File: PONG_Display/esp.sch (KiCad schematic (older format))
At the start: 15 parts, among them J8 ESP_Conn, J9 ESP_Prog_Conn, Q1 BSS138, Q2 BSS138, SW2 SW_Push, SW3 SW_Push_SPDT, SW4 SW_Push_SPDT

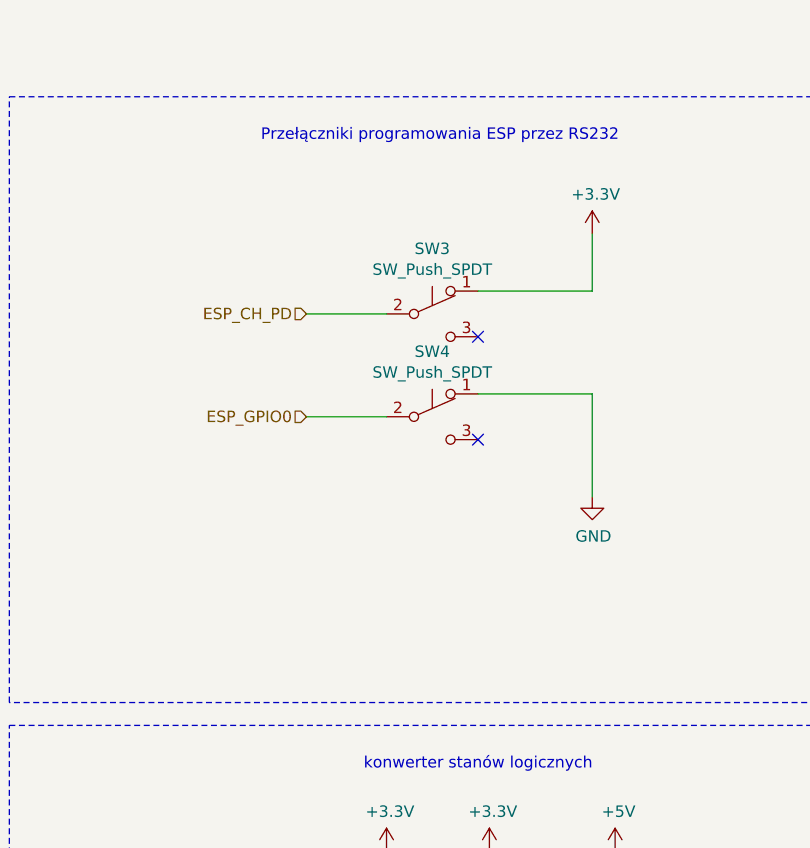
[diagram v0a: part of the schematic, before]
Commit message: Updated GPIO pins in ESP schematic
Connected GPIO2 to VDD with pull-up resistor and changed switches wiring
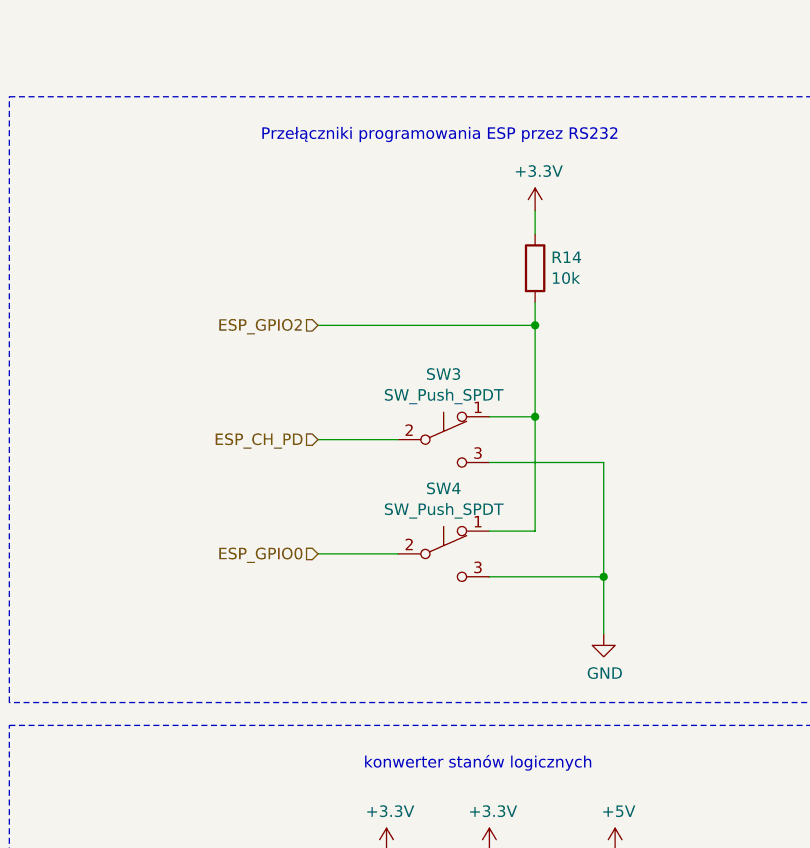
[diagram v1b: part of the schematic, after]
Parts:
- added R14: 10k, symbol Device:R
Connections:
- net +3V3: now also R14.1; no longer SW3.1 (A)
- net ESP_GPIO2: now also SW3.1 (A), SW4.1 (A), R14.2
- net GND: now also SW3.3 (C), SW4.3 (C); no longer SW4.1 (A)
- no-connect marks 2 -> 0
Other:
- moved on the sheet: SW3, SW4
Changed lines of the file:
@@
 L power:+3.3V #PWR068
 U 1 1 5E9D6E89
-P 9550 1900
-F 0 "#PWR068" H 9550 1750 50  0001 C CNN
-F 1 "+3.3V" H 9565 2073 50  0000 C CNN
-F 2 "" H 9550 1900 50  0001 C CNN
-F 3 "" H 9550 1900 50  0001 C CNN
-	1    9550 1900
+P 9300 1800
+F 0 "#PWR068" H 9300 1650 50  0001 C CNN
+F 1 "+3.3V" H 9315 1973 50  0000 C CNN
+F 2 "" H 9300 1800 50  0001 C CNN
+F 3 "" H 9300 1800 50  0001 C CNN
+	1    9300 1800
 	1    0    0    -1
 $EndComp
@@
 L power:GND #PWR069
 U 1 1 5E9D779A
-P 9550 3050
-F 0 "#PWR069" H 9550 2800 50  0001 C CNN
-F 1 "GND" H 9555 2877 50  0000 C CNN
-F 2 "" H 9550 3050 50  0001 C CNN
-F 3 "" H 9550 3050 50  0001 C CNN
-	1    9550 3050
-	1    0    0    -1
-$EndComp
-Wire Wire Line
-	9550 1900 9550 2150
-Wire Wire Line
-	9550 2150 9050 2150
-Wire Wire Line
-	9050 2600 9550 2600
-Wire Wire Line
-	9550 2600 9550 3050
-Wire Wire Line
-	8300 2250 8650 2250
-Wire Wire Line
-	8300 2700 8650 2700
+P 9600 3650
+F 0 "#PWR069" H 9600 3400 50  0001 C CNN
+F 1 "GND" H 9605 3477 50  0000 C CNN
+F 2 "" H 9600 3650 50  0001 C CNN
+F 3 "" H 9600 3650 50  0001 C CNN
+	1    9600 3650
+	1    0    0    -1
+$EndComp
+Wire Wire Line
+	8350 2800 8700 2800
+Wire Wire Line
+	8350 3300 8700 3300
 $Comp
 L Switch:SW_Push_SPDT SW3
 U 1 1 5E9E35EF
-P 8850 2250
-F 0 "SW3" H 8850 2535 50  0000 C CNN
-F 1 "SW_Push_SPDT" H 8850 2444 50  0000 C CNN
-F 2 "LIB_PONG_Display:SPDT_switch" H 8850 2250 50  0001 C CNN
-F 3 "~" H 8850 2250 50  0001 C CNN
-	1    8850 2250
-	1    0    0    -1
-$EndComp
-$Comp
-L Switch:SW_Push_SPDT SW4
-U 1 1 5E9E3E9D
-P 8850 2700
-F 0 "SW4" H 8850 2985 50  0000 C CNN
-F 1 "SW_Push_SPDT" H 8850 2894 50  0000 C CNN
-F 2 "LIB_PONG_Display:SPDT_switch" H 8850 2700 50  0001 C CNN
-F 3 "~" H 8850 2700 50  0001 C CNN
-	1    8850 2700
+P 8900 2800
+F 0 "SW3" H 8900 3085 50  0000 C CNN
+F 1 "SW_Push_SPDT" H 8900 2994 50  0000 C CNN
+F 2 "LIB_PONG_Display:SPDT_switch" H 8900 2800 50  0001 C CNN
+F 3 "~" H 8900 2800 50  0001 C CNN
+	1    8900 2800
 	1    0    0    -1
 $EndComp
@@
 Text HLabel 3950 2250 0    50   Input ~ 0
 ESP_GPIO2
-Text HLabel 8300 2250 0    50   Input ~ 0
+Text HLabel 8350 2800 0    50   Input ~ 0
 ESP_CH_PD
-Text HLabel 8300 2700 0    50   Input ~ 0
+Text HLabel 8350 3300 0    50   Input ~ 0
 ESP_GPIO0
-NoConn ~ 9050 2350
-NoConn ~ 9050 2800
 $Comp
 L power:GND #PWR065
@@
 Text Notes 3500 4650 0    50   ~ 0
 Przycisk resetu układu ESP
+Text HLabel 8350 2300 0    50   Input ~ 0
+ESP_GPIO2
+$Comp
+L Switch:SW_Push_SPDT SW4
+U 1 1 5E9E3E9D
+P 8900 3300
+F 0 "SW4" H 8900 3585 50  0000 C CNN
+F 1 "SW_Push_SPDT" H 8900 3494 50  0000 C CNN
+F 2 "LIB_PONG_Display:SPDT_switch" H 8900 3300 50  0001 C CNN
+F 3 "~" H 8900 3300 50  0001 C CNN
+	1    8900 3300
+	1    0    0    -1
+$EndComp
+Wire Wire Line
+	9600 2900 9100 2900
+$Comp
+L Device:R R14
+U 1 1 5EA47580
+P 9300 2050
+F 0 "R14" H 9370 2096 50  0000 L CNN
+F 1 "10k" H 9370 2005 50  0000 L CNN
+F 2 "" V 9230 2050 50  0001 C CNN
+F 3 "~" H 9300 2050 50  0001 C CNN
+	1    9300 2050
+	1    0    0    -1
+$EndComp
+Wire Wire Line
+	9600 2900 9600 3400
+Wire Wire Line
+	9100 3400 9600 3400
+Connection ~ 9600 3400
+Wire Wire Line
+	9600 3400 9600 3650
+Wire Wire Line
+	8350 2300 9300 2300
+Wire Wire Line
+	9300 2300 9300 2700
+Wire Wire Line
+	9300 2700 9100 2700
+Wire Wire Line
+	9100 3200 9300 3200
+Wire Wire Line
+	9300 3200 9300 2700
+Connection ~ 9300 2700
+Wire Wire Line
+	9300 1900 9300 1800
+Wire Wire Line
+	9300 2200 9300 2300
+Connection ~ 9300 2300
 $EndSCHEMATC

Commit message: layout4
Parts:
- R14: footprint (none) -> Resistor_SMD:R_0603_1608Metric_Pad1.05x0.95mm_HandSolder
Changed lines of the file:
@@
 F 0 "R14" H 9370 2096 50  0000 L CNN
 F 1 "10k" H 9370 2005 50  0000 L CNN
-F 2 "" V 9230 2050 50  0001 C CNN
+F 2 "Resistor_SMD:R_0603_1608Metric_Pad1.05x0.95mm_HandSolder" V 9230 2050 50  0001 C CNN
 F 3 "~" H 9300 2050 50  0001 C CNN
 	1    9300 2050

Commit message: layout8
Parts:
- added SW6: SW_Push_SPDT, LIB_PONG_Display:SPDT_switch, symbol Switch:SW_Push_SPDT
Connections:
- net +3V3: now also SW6.1 (A); no longer J9.1 (Pin_1)
- new net: J9.1 (Pin_1), SW6.2 (B)
- no-connect marks 0 -> 1
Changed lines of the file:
@@
 L power:+3.3V #PWR062
 U 1 1 5E859CE6
-P 4350 2900
-F 0 "#PWR062" H 4350 2750 50  0001 C CNN
-F 1 "+3.3V" H 4365 3073 50  0000 C CNN
-F 2 "" H 4350 2900 50  0001 C CNN
-F 3 "" H 4350 2900 50  0001 C CNN
-	1    4350 2900
+P 5200 2600
+F 0 "#PWR062" H 5200 2450 50  0001 C CNN
+F 1 "+3.3V" H 5215 2773 50  0000 C CNN
+F 2 "" H 5200 2600 50  0001 C CNN
+F 3 "" H 5200 2600 50  0001 C CNN
+	1    5200 2600
 	1    0    0    -1
 $EndComp
@@
 	1    0    0    -1
 $EndComp
-Wire Wire Line
-	4350 2900 4350 3050
 Wire Wire Line
 	4350 3350 4350 3600
@@
 	9300 2200 9300 2300
 Connection ~ 9300 2300
+$Comp
+L Switch:SW_Push_SPDT SW6
+U 1 1 5EAD59E6
+P 4800 2800
+F 0 "SW6" H 4800 3085 50  0000 C CNN
+F 1 "SW_Push_SPDT" H 4800 2994 50  0000 C CNN
+F 2 "LIB_PONG_Display:SPDT_switch" H 4800 2800 50  0001 C CNN
+F 3 "~" H 4800 2800 50  0001 C CNN
+	1    4800 2800
+	1    0    0    -1
+$EndComp
+NoConn ~ 5000 2900
+Wire Wire Line
+	5000 2700 5200 2700
+Wire Wire Line
+	5200 2700 5200 2600
+Wire Wire Line
+	4350 2800 4600 2800
+Wire Wire Line
+	4350 2800 4350 3050
 $EndSCHEMATC

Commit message: layout9
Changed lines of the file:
@@
 Text Notes 3400 1500 0    50   ~ 0
 Złącze do modułu WiFi oraz programatora RS232
-Text Label 3000 1050 0    50   ~ 0
-Do_sprawdzenia_przed_rysowaniem_pcb_czy_na_pewno_piny_dobrze_przypisane
 Wire Notes Line
 	2650 1300 6100 1300
